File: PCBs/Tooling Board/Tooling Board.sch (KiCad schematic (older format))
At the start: 9 parts

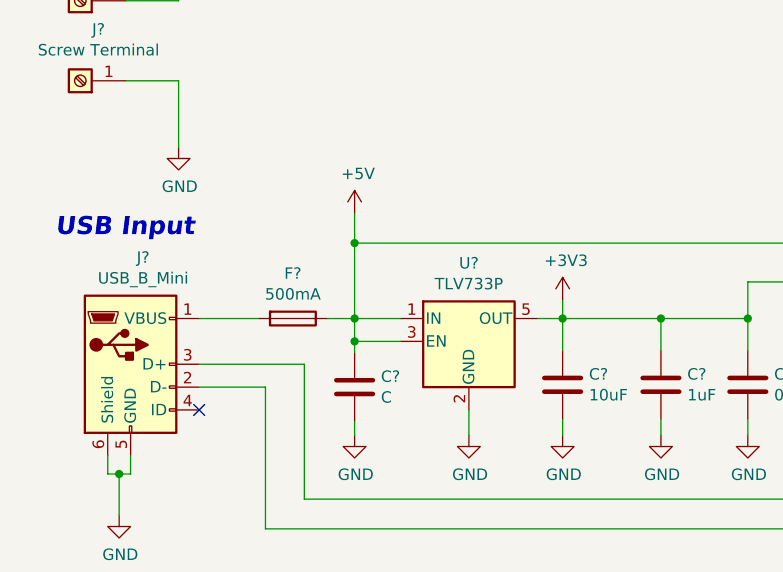
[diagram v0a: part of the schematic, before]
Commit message: Add DC Motor Control
-Added H-bridge drivers and logic inverters
-Should be able to control up to 6 DC motors / other loads
-We'll see if we can fit 3 chips on the board (we should be able to)
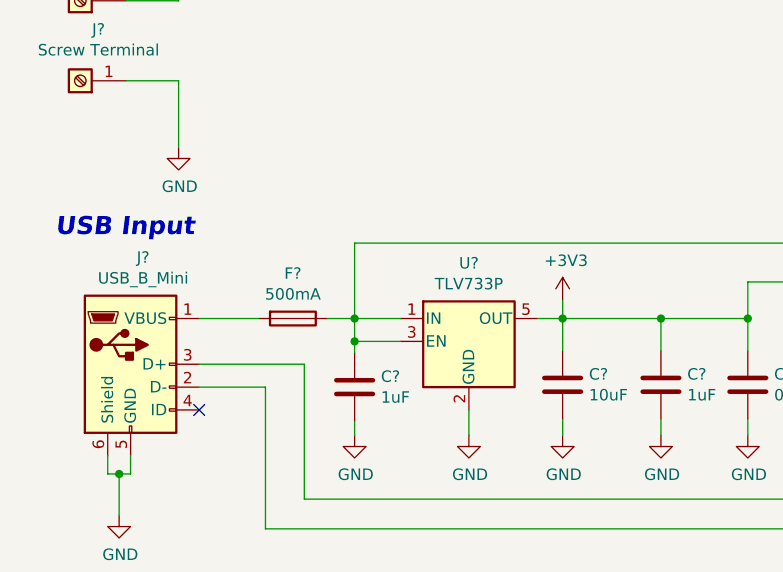
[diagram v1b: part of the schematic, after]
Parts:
- C?: value C -> 1uF
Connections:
- net +5V renamed MicroController/+5V
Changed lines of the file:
@@
 $Descr A4 11693 8268
 encoding utf-8
-Sheet 1 4
+Sheet 1 7
 Title ""
 Date ""
@@
 Wire Wire Line
 	2380 2940 2500 2940
-Wire Wire Line
-	2500 2610 2500 2480
-Connection ~ 2500 2610
-$Comp
-L power:+5V #PWR?
-U 1 1 5C4B8B73
-P 2500 2480
-F 0 "#PWR?" H 2500 2330 50  0001 C CNN
-F 1 "+5V" H 2515 2653 50  0000 C CNN
-F 2 "" H 2500 2480 50  0001 C CNN
-F 3 "" H 2500 2480 50  0001 C CNN
-	1    2500 2480
-	1    0    0    -1
-$EndComp
 NoConn ~ 1820 3340
 Wire Wire Line
@@
 P 2500 3240
 F 0 "C?" H 2615 3286 50  0000 L CNN
-F 1 "C" H 2615 3195 50  0000 L CNN
+F 1 "1uF" H 2615 3195 50  0000 L CNN
 F 2 "" H 2538 3090 50  0001 C CNN
 F 3 "~" H 2500 3240 50  0001 C CNN

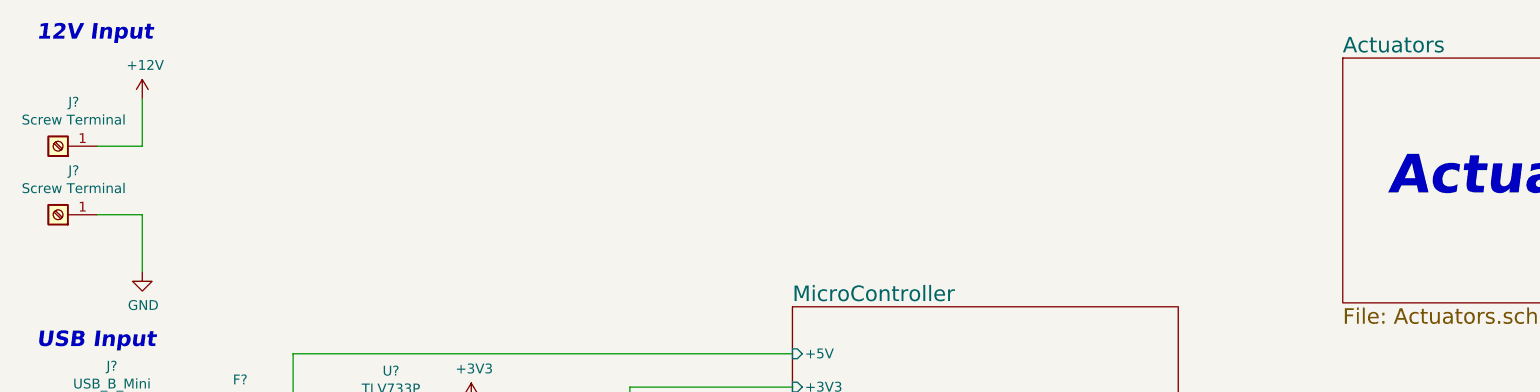
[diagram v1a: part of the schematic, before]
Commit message: Finished Actuator Section
-Added Dual LED Control
-Spec'd fets for nmos in LED circuit
-Still need to map all control pins
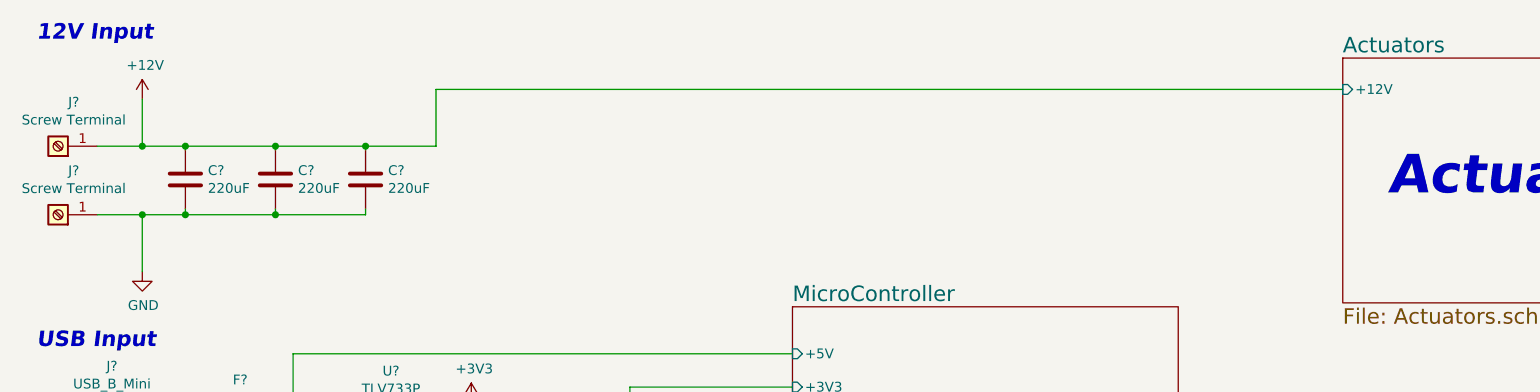
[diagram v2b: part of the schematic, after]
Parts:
- added C? (x3): 220uF, symbol Device:C
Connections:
- net +12V: now also C?.1, C?.1, C?.1
- net GND: now also C?.2, C?.2, C?.2
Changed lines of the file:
@@
 F0 "Actuators" 79
 F1 "Actuators.sch" 79
+F2 "+12V" I L 7860 1260 50
 $EndSheet
 $Sheet
@@
 Wire Wire Line
 	2110 3240 1820 3240
+$Comp
+L Device:C C?
+U 1 1 5C4D7023
+P 1950 1720
+F 0 "C?" H 2065 1766 50  0000 L CNN
+F 1 "220uF" H 2065 1675 50  0000 L CNN
+F 2 "" H 1988 1570 50  0001 C CNN
+F 3 "~" H 1950 1720 50  0001 C CNN
+	1    1950 1720
+	1    0    0    -1
+$EndComp
+$Comp
+L Device:C C?
+U 1 1 5C4D7167
+P 2410 1720
+F 0 "C?" H 2525 1766 50  0000 L CNN
+F 1 "220uF" H 2525 1675 50  0000 L CNN
+F 2 "" H 2448 1570 50  0001 C CNN
+F 3 "~" H 2410 1720 50  0001 C CNN
+	1    2410 1720
+	1    0    0    -1
+$EndComp
+$Comp
+L Device:C C?
+U 1 1 5C4D7199
+P 2870 1720
+F 0 "C?" H 2985 1766 50  0000 L CNN
+F 1 "220uF" H 2985 1675 50  0000 L CNN
+F 2 "" H 2908 1570 50  0001 C CNN
+F 3 "~" H 2870 1720 50  0001 C CNN
+	1    2870 1720
+	1    0    0    -1
+$EndComp
+Wire Wire Line
+	1950 1570 1950 1550
+Wire Wire Line
+	1950 1550 1730 1550
+Connection ~ 1730 1550
+Wire Wire Line
+	1950 1550 2410 1550
+Wire Wire Line
+	2410 1550 2410 1570
+Connection ~ 1950 1550
+Wire Wire Line
+	2410 1550 2870 1550
+Wire Wire Line
+	2870 1550 2870 1570
+Connection ~ 2410 1550
+Wire Wire Line
+	1950 1870 1950 1900
+Wire Wire Line
+	1950 1900 1730 1900
+Connection ~ 1730 1900
+Wire Wire Line
+	2410 1870 2410 1900
+Wire Wire Line
+	2410 1900 1950 1900
+Connection ~ 1950 1900
+Wire Wire Line
+	2870 1870 2870 1900
+Wire Wire Line
+	2870 1900 2410 1900
+Connection ~ 2410 1900
+Wire Wire Line
+	2870 1550 3230 1550
+Wire Wire Line
+	3230 1550 3230 1260
+Wire Wire Line
+	3230 1260 7860 1260
+Connection ~ 2870 1550
 $EndSCHEMATC

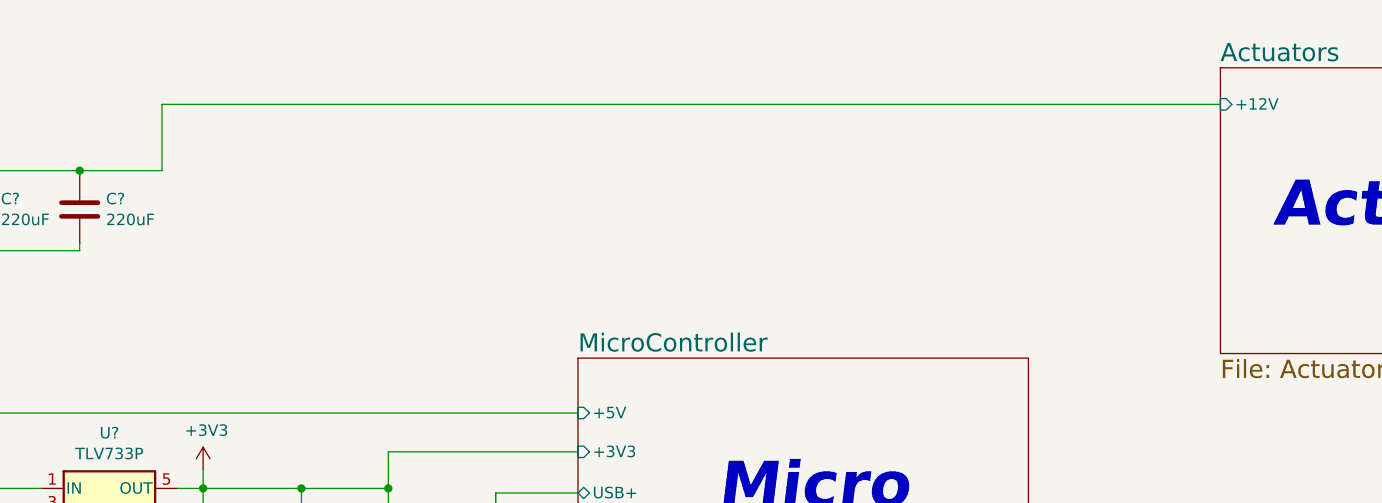
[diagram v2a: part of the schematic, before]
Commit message: Added Sensors
-Added pH Circuit and spec'd components
-Added Pressure sensor connecter
-Added External Temp sensor connector
-Added metal detector connector + input circuit

Need to add IMU interface now (not hard)
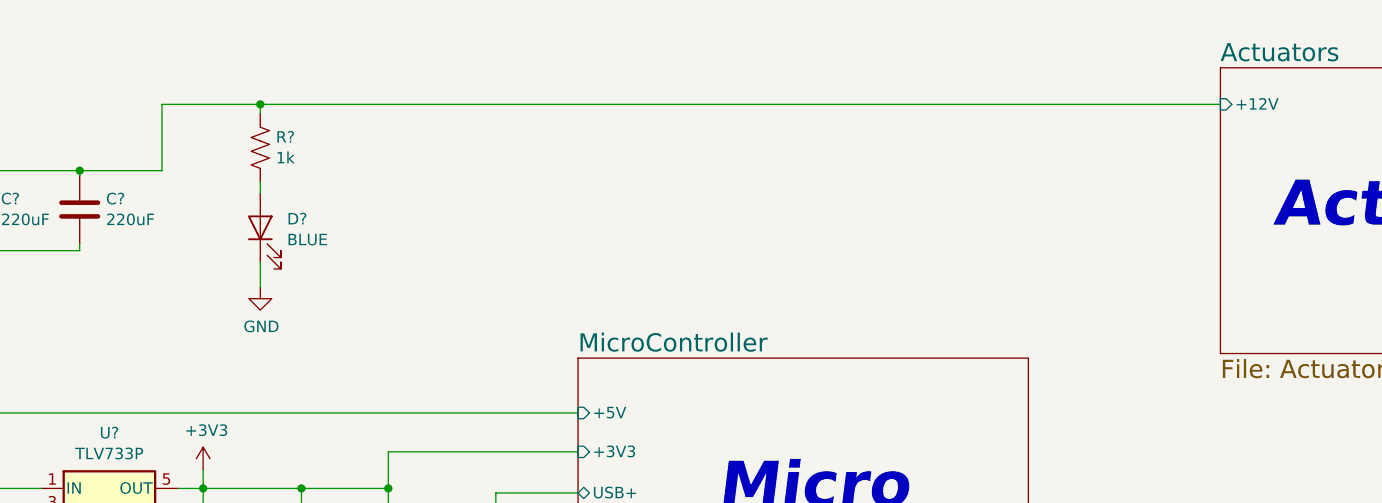
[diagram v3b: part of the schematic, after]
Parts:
- added D?: BLUE, symbol Device:LED
- added R?: 1k, symbol Device:R_US
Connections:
- net +12V: now also R?.1
- net GND: now also D?.1 (K)
- new net: D?.2 (A), R?.2
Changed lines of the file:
@@
 $Descr A4 11693 8268
 encoding utf-8
-Sheet 1 7
+Sheet 1 8
 Title ""
 Date ""
@@
 	3230 1550 3230 1260
 Wire Wire Line
-	3230 1260 7860 1260
+	3230 1260 3660 1260
 Connection ~ 2870 1550
+$Comp
+L Device:LED D?
+U 1 1 5C529958
+P 3660 1800
+F 0 "D?" V 3698 1683 50  0000 R CNN
+F 1 "BLUE" V 3607 1683 50  0000 R CNN
+F 2 "" H 3660 1800 50  0001 C CNN
+F 3 "~" H 3660 1800 50  0001 C CNN
+	1    3660 1800
+	0    -1   -1   0
+$EndComp
+$Comp
+L power:GND #PWR?
+U 1 1 5C529A77
+P 3660 2060
+F 0 "#PWR?" H 3660 1810 50  0001 C CNN
+F 1 "GND" H 3665 1887 50  0000 C CNN
+F 2 "" H 3660 2060 50  0001 C CNN
+F 3 "" H 3660 2060 50  0001 C CNN
+	1    3660 2060
+	1    0    0    -1
+$EndComp
+Wire Wire Line
+	3660 2060 3660 1950
+$Comp
+L Device:R_US R?
+U 1 1 5C52AA47
+P 3660 1450
+F 0 "R?" H 3728 1496 50  0000 L CNN
+F 1 "1k" H 3728 1405 50  0000 L CNN
+F 2 "" V 3700 1440 50  0001 C CNN
+F 3 "~" H 3660 1450 50  0001 C CNN
+	1    3660 1450
+	1    0    0    -1
+$EndComp
+Wire Wire Line
+	3660 1650 3660 1600
+Wire Wire Line
+	3660 1300 3660 1260
+Connection ~ 3660 1260
+Wire Wire Line
+	3660 1260 7860 1260
 $EndSCHEMATC

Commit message: Added Footprints
-Whoooo boy here we go
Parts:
- C101, C102, C104: renamed from C?; footprint (none) -> Capacitors_THT:CP_Radial_D6.3mm_P2.50mm
- C103, C105, C106, C107: renamed from C?; footprint (none) -> Capacitors_SMD:C_0805_HandSoldering
- D101: renamed from D?; footprint (none) -> LEDs:LED_0805_HandSoldering
- F101: renamed from F?; footprint (none) -> EER:Fuse_SMD1206_Reflow
- J101, J102: renamed from J?; footprint (none) -> EER:RingTerminal
- J103: renamed from J?; footprint (none) -> EER:32005-201
- R101: renamed from R?; footprint (none) -> Resistors_SMD:R_0805_HandSoldering
- U101: renamed from U?; footprint Package_TO_SOT_SMD:SOT-23-5 -> TO_SOT_Packages_SMD:SOT-23-5
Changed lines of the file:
@@
 Sensors
 $Comp
-L Connector:Screw_Terminal_01x01 J?
+L Connector:Screw_Terminal_01x01 J101
 U 1 1 5C4A7AB1
 P 1300 1550
-F 0 "J?" H 1220 1325 50  0000 C CNN
+F 0 "J101" H 1220 1325 50  0000 C CNN
 F 1 "Screw Terminal" H 1220 1416 50  0000 C CNN
-F 2 "" H 1300 1550 50  0001 C CNN
+F 2 "EER:RingTerminal" H 1300 1550 50  0001 C CNN
 F 3 "~" H 1300 1550 50  0001 C CNN
 	1    1300 1550
@@
 $EndComp
 $Comp
-L Connector:Screw_Terminal_01x01 J?
+L Connector:Screw_Terminal_01x01 J102
 U 1 1 5C4A7AFB
 P 1300 1900
-F 0 "J?" H 1220 1675 50  0000 C CNN
+F 0 "J102" H 1220 1675 50  0000 C CNN
 F 1 "Screw Terminal" H 1220 1766 50  0000 C CNN
-F 2 "" H 1300 1900 50  0001 C CNN
+F 2 "EER:RingTerminal" H 1300 1900 50  0001 C CNN
 F 3 "~" H 1300 1900 50  0001 C CNN
 	1    1300 1900
@@
 	1730 1550 1730 1310
 $Comp
-L power:+12V #PWR?
+L power:+12V #PWR0101
 U 1 1 5C4A7BCA
 P 1730 1310
-F 0 "#PWR?" H 1730 1160 50  0001 C CNN
+F 0 "#PWR0101" H 1730 1160 50  0001 C CNN
 F 1 "+12V" H 1745 1483 50  0000 C CNN
 F 2 "" H 1730 1310 50  0001 C CNN
@@
 $EndComp
 $Comp
-L power:GND #PWR?
+L power:GND #PWR0102
 U 1 1 5C4A7C05
 P 1730 2190
-F 0 "#PWR?" H 1730 1940 50  0001 C CNN
+F 0 "#PWR0102" H 1730 1940 50  0001 C CNN
 F 1 "GND" H 1735 2017 50  0000 C CNN
 F 2 "" H 1730 2190 50  0001 C CNN
@@
 USB Input
 $Comp
-L Connector:USB_B_Mini J?
+L Connector:USB_B_Mini J103
 U 1 1 5C4B5D01
 P 1520 3140
-F 0 "J?" H 1575 3607 50  0000 C CNN
+F 0 "J103" H 1575 3607 50  0000 C CNN
 F 1 "USB_B_Mini" H 1575 3516 50  0000 C CNN
-F 2 "" H 1670 3090 50  0001 C CNN
+F 2 "EER:32005-201" H 1670 3090 50  0001 C CNN
 F 3 "~" H 1670 3090 50  0001 C CNN
 	1    1520 3140
@@
 $EndComp
 $Comp
-L Device:Fuse F?
+L Device:Fuse F101
 U 1 1 5C4B8A3E
 P 2230 2940
-F 0 "F?" V 2033 2940 50  0000 C CNN
+F 0 "F101" V 2033 2940 50  0000 C CNN
 F 1 "500mA" V 2124 2940 50  0000 C CNN
-F 2 "" V 2160 2940 50  0001 C CNN
+F 2 "EER:Fuse_SMD1206_Reflow" V 2160 2940 50  0001 C CNN
 F 3 "~" H 2230 2940 50  0001 C CNN
 	1    2230 2940
@@
 	1470 3620 1520 3620
 $Comp
-L power:GND #PWR?
+L power:GND #PWR0103
 U 1 1 5C4B8D61
 P 1470 3800
-F 0 "#PWR?" H 1470 3550 50  0001 C CNN
+F 0 "#PWR0103" H 1470 3550 50  0001 C CNN
 F 1 "GND" H 1475 3627 50  0000 C CNN
 F 2 "" H 1470 3800 50  0001 C CNN
@@
 	2500 2610 5050 2610
 $Comp
-L Regulator_Linear:TLV70018_SOT23-5 U?
+L Regulator_Linear:TLV70018_SOT23-5 U101
 U 1 1 5C4B9BB4
 P 3000 3040
-F 0 "U?" H 3000 3382 50  0000 C CNN
+F 0 "U101" H 3000 3382 50  0000 C CNN
 F 1 "TLV733P" H 3000 3291 50  0000 C CNN
-F 2 "Package_TO_SOT_SMD:SOT-23-5" H 3000 3365 50  0001 C CIN
+F 2 "TO_SOT_Packages_SMD:SOT-23-5" H 3000 3365 50  0001 C CIN
 F 3 "296-40673-1-ND" H 3000 3090 50  0001 C CNN
 	1    3000 3040
@@
 	2500 3040 2700 3040
 $Comp
-L Device:C C?
+L Device:C C103
 U 1 1 5C4BA13E
 P 2500 3240
-F 0 "C?" H 2615 3286 50  0000 L CNN
+F 0 "C103" H 2615 3286 50  0000 L CNN
 F 1 "1uF" H 2615 3195 50  0000 L CNN
-F 2 "" H 2538 3090 50  0001 C CNN
+F 2 "Capacitors_SMD:C_0805_HandSoldering" H 2538 3090 50  0001 C CNN
 F 3 "~" H 2500 3240 50  0001 C CNN
 	1    2500 3240
@@
 $EndComp
 $Comp
-L Device:C C?
+L Device:C C105
 U 1 1 5C4BA186
 P 3410 3230
-F 0 "C?" H 3525 3276 50  0000 L CNN
+F 0 "C105" H 3525 3276 50  0000 L CNN
 F 1 "10uF" H 3525 3185 50  0000 L CNN
-F 2 "" H 3448 3080 50  0001 C CNN
+F 2 "Capacitors_SMD:C_0805_HandSoldering" H 3448 3080 50  0001 C CNN
 F 3 "~" H 3410 3230 50  0001 C CNN
 	1    3410 3230
@@
 Connection ~ 3410 2940
 $Comp
-L power:+3V3 #PWR?
+L power:+3V3 #PWR0104
 U 1 1 5C4BA9F9
 P 3410 2860
-F 0 "#PWR?" H 3410 2710 50  0001 C CNN
+F 0 "#PWR0104" H 3410 2710 50  0001 C CNN
 F 1 "+3V3" H 3425 3033 50  0000 C CNN
 F 2 "" H 3410 2860 50  0001 C CNN
@@
 	3410 2860 3410 2940
 $Comp
-L power:GND #PWR?
+L power:GND #PWR0105
 U 1 1 5C4BB142
 P 2500 3450
-F 0 "#PWR?" H 2500 3200 50  0001 C CNN
+F 0 "#PWR0105" H 2500 3200 50  0001 C CNN
 F 1 "GND" H 2505 3277 50  0000 C CNN
 F 2 "" H 2500 3450 50  0001 C CNN
@@
 $EndComp
 $Comp
-L power:GND #PWR?
+L power:GND #PWR0106
 U 1 1 5C4BB15B
 P 3000 3450
-F 0 "#PWR?" H 3000 3200 50  0001 C CNN
+F 0 "#PWR0106" H 3000 3200 50  0001 C CNN
 F 1 "GND" H 3005 3277 50  0000 C CNN
 F 2 "" H 3000 3450 50  0001 C CNN
@@
 $EndComp
 $Comp
-L power:GND #PWR?
+L power:GND #PWR0107
 U 1 1 5C4BB174
 P 3840 3450
-F 0 "#PWR?" H 3840 3200 50  0001 C CNN
+F 0 "#PWR0107" H 3840 3200 50  0001 C CNN
 F 1 "GND" H 3845 3277 50  0000 C CNN
 F 2 "" H 3840 3450 50  0001 C CNN
@@
 	3000 3340 3000 3450
 $Comp
-L Device:C C?
+L Device:C C106
 U 1 1 5C4BB6C4
 P 3840 3230
-F 0 "C?" H 3955 3276 50  0000 L CNN
+F 0 "C106" H 3955 3276 50  0000 L CNN
 F 1 "1uF" H 3955 3185 50  0000 L CNN
-F 2 "" H 3878 3080 50  0001 C CNN
+F 2 "Capacitors_SMD:C_0805_HandSoldering" H 3878 3080 50  0001 C CNN
 F 3 "~" H 3840 3230 50  0001 C CNN
 	1    3840 3230
@@
 $EndComp
 $Comp
-L Device:C C?
+L Device:C C107
 U 1 1 5C4BB81D
 P 4220 3230
-F 0 "C?" H 4335 3276 50  0000 L CNN
+F 0 "C107" H 4335 3276 50  0000 L CNN
 F 1 "0.1uF" H 4335 3185 50  0000 L CNN
-F 2 "" H 4258 3080 50  0001 C CNN
+F 2 "Capacitors_SMD:C_0805_HandSoldering" H 4258 3080 50  0001 C CNN
 F 3 "~" H 4220 3230 50  0001 C CNN
 	1    4220 3230
@@
 Connection ~ 3840 2940
 $Comp
-L power:GND #PWR?
+L power:GND #PWR0108
 U 1 1 5C4BC46D
 P 3410 3450
-F 0 "#PWR?" H 3410 3200 50  0001 C CNN
+F 0 "#PWR0108" H 3410 3200 50  0001 C CNN
 F 1 "GND" H 3415 3277 50  0000 C CNN
 F 2 "" H 3410 3450 50  0001 C CNN
@@
 $EndComp
 $Comp
-L power:GND #PWR?
+L power:GND #PWR0109
 U 1 1 5C4BC48A
 P 4220 3450
-F 0 "#PWR?" H 4220 3200 50  0001 C CNN
+F 0 "#PWR0109" H 4220 3200 50  0001 C CNN
 F 1 "GND" H 4225 3277 50  0000 C CNN
 F 2 "" H 4220 3450 50  0001 C CNN
@@
 	2110 3240 1820 3240
 $Comp
-L Device:C C?
+L Device:C C101
 U 1 1 5C4D7023
 P 1950 1720
-F 0 "C?" H 2065 1766 50  0000 L CNN
+F 0 "C101" H 2065 1766 50  0000 L CNN
 F 1 "220uF" H 2065 1675 50  0000 L CNN
-F 2 "" H 1988 1570 50  0001 C CNN
+F 2 "Capacitors_THT:CP_Radial_D6.3mm_P2.50mm" H 1988 1570 50  0001 C CNN
 F 3 "~" H 1950 1720 50  0001 C CNN
 	1    1950 1720
@@
 $EndComp
 $Comp
-L Device:C C?
+L Device:C C102
 U 1 1 5C4D7167
 P 2410 1720
-F 0 "C?" H 2525 1766 50  0000 L CNN
+F 0 "C102" H 2525 1766 50  0000 L CNN
 F 1 "220uF" H 2525 1675 50  0000 L CNN
-F 2 "" H 2448 1570 50  0001 C CNN
+F 2 "Capacitors_THT:CP_Radial_D6.3mm_P2.50mm" H 2448 1570 50  0001 C CNN
 F 3 "~" H 2410 1720 50  0001 C CNN
 	1    2410 1720
@@
 $EndComp
 $Comp
-L Device:C C?
+L Device:C C104
 U 1 1 5C4D7199
 P 2870 1720
-F 0 "C?" H 2985 1766 50  0000 L CNN
+F 0 "C104" H 2985 1766 50  0000 L CNN
 F 1 "220uF" H 2985 1675 50  0000 L CNN
-F 2 "" H 2908 1570 50  0001 C CNN
+F 2 "Capacitors_THT:CP_Radial_D6.3mm_P2.50mm" H 2908 1570 50  0001 C CNN
 F 3 "~" H 2870 1720 50  0001 C CNN
 	1    2870 1720
@@
 Connection ~ 2870 1550
 $Comp
-L Device:LED D?
+L Device:LED D101
 U 1 1 5C529958
 P 3660 1800
-F 0 "D?" V 3698 1683 50  0000 R CNN
+F 0 "D101" V 3698 1683 50  0000 R CNN
 F 1 "BLUE" V 3607 1683 50  0000 R CNN
-F 2 "" H 3660 1800 50  0001 C CNN
+F 2 "LEDs:LED_0805_HandSoldering" H 3660 1800 50  0001 C CNN
 F 3 "~" H 3660 1800 50  0001 C CNN
 	1    3660 1800
@@
 $EndComp
 $Comp
-L power:GND #PWR?
+L power:GND #PWR0110
 U 1 1 5C529A77
 P 3660 2060
-F 0 "#PWR?" H 3660 1810 50  0001 C CNN
+F 0 "#PWR0110" H 3660 1810 50  0001 C CNN
 F 1 "GND" H 3665 1887 50  0000 C CNN
 F 2 "" H 3660 2060 50  0001 C CNN
@@
 	3660 2060 3660 1950
 $Comp
-L Device:R_US R?
+L Device:R_US R101
 U 1 1 5C52AA47
 P 3660 1450
-F 0 "R?" H 3728 1496 50  0000 L CNN
+F 0 "R101" H 3728 1496 50  0000 L CNN
 F 1 "1k" H 3728 1405 50  0000 L CNN
-F 2 "" V 3700 1440 50  0001 C CNN
+F 2 "Resistors_SMD:R_0805_HandSoldering" V 3700 1440 50  0001 C CNN
 F 3 "~" H 3660 1450 50  0001 C CNN
 	1    3660 1450

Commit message: Almost Finished
-Still going, help
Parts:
- C103, C105, C106, C107: footprint Capacitors_SMD:C_0805_HandSoldering -> Capacitors_SMD:C_0805
- D101: footprint LEDs:LED_0805_HandSoldering -> LEDs:LED_0805
- R101: footprint Resistors_SMD:R_0805_HandSoldering -> Resistors_SMD:R_0805
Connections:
- net MicroController/+5V renamed MicroController/+5V_IN
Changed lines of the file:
@@
 F0 "MicroController" 79
 F1 "MicroController.sch" 79
-F2 "+5V" I L 5050 2610 50
+F2 "+5V_IN" I L 5050 2610 50
 F3 "+3V3" I L 5050 2780 50
 F4 "USB+" B L 5050 2960 50
@@
 F 0 "C103" H 2615 3286 50  0000 L CNN
 F 1 "1uF" H 2615 3195 50  0000 L CNN
-F 2 "Capacitors_SMD:C_0805_HandSoldering" H 2538 3090 50  0001 C CNN
+F 2 "Capacitors_SMD:C_0805" H 2538 3090 50  0001 C CNN
 F 3 "~" H 2500 3240 50  0001 C CNN
 	1    2500 3240
@@
 F 0 "C105" H 3525 3276 50  0000 L CNN
 F 1 "10uF" H 3525 3185 50  0000 L CNN
-F 2 "Capacitors_SMD:C_0805_HandSoldering" H 3448 3080 50  0001 C CNN
+F 2 "Capacitors_SMD:C_0805" H 3448 3080 50  0001 C CNN
 F 3 "~" H 3410 3230 50  0001 C CNN
 	1    3410 3230
@@
 F 0 "C106" H 3955 3276 50  0000 L CNN
 F 1 "1uF" H 3955 3185 50  0000 L CNN
-F 2 "Capacitors_SMD:C_0805_HandSoldering" H 3878 3080 50  0001 C CNN
+F 2 "Capacitors_SMD:C_0805" H 3878 3080 50  0001 C CNN
 F 3 "~" H 3840 3230 50  0001 C CNN
 	1    3840 3230
@@
 F 0 "C107" H 4335 3276 50  0000 L CNN
 F 1 "0.1uF" H 4335 3185 50  0000 L CNN
-F 2 "Capacitors_SMD:C_0805_HandSoldering" H 4258 3080 50  0001 C CNN
+F 2 "Capacitors_SMD:C_0805" H 4258 3080 50  0001 C CNN
 F 3 "~" H 4220 3230 50  0001 C CNN
 	1    4220 3230
@@
 F 0 "D101" V 3698 1683 50  0000 R CNN
 F 1 "BLUE" V 3607 1683 50  0000 R CNN
-F 2 "LEDs:LED_0805_HandSoldering" H 3660 1800 50  0001 C CNN
+F 2 "LEDs:LED_0805" H 3660 1800 50  0001 C CNN
 F 3 "~" H 3660 1800 50  0001 C CNN
 	1    3660 1800
@@
 F 0 "R101" H 3728 1496 50  0000 L CNN
 F 1 "1k" H 3728 1405 50  0000 L CNN
-F 2 "Resistors_SMD:R_0805_HandSoldering" V 3700 1440 50  0001 C CNN
+F 2 "Resistors_SMD:R_0805" V 3700 1440 50  0001 C CNN
 F 3 "~" H 3660 1450 50  0001 C CNN
 	1    3660 1450
